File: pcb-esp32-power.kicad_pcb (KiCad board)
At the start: 2 copper layers, 75 x 34 mm, 36 parts, among them IC1 IP5108, IC2 SY8008B, J1 DB9_Female, J2 Conn_01x02, J3 Conn_01x14, J4 Conn_01x16, U1 STEPDOWN12_5

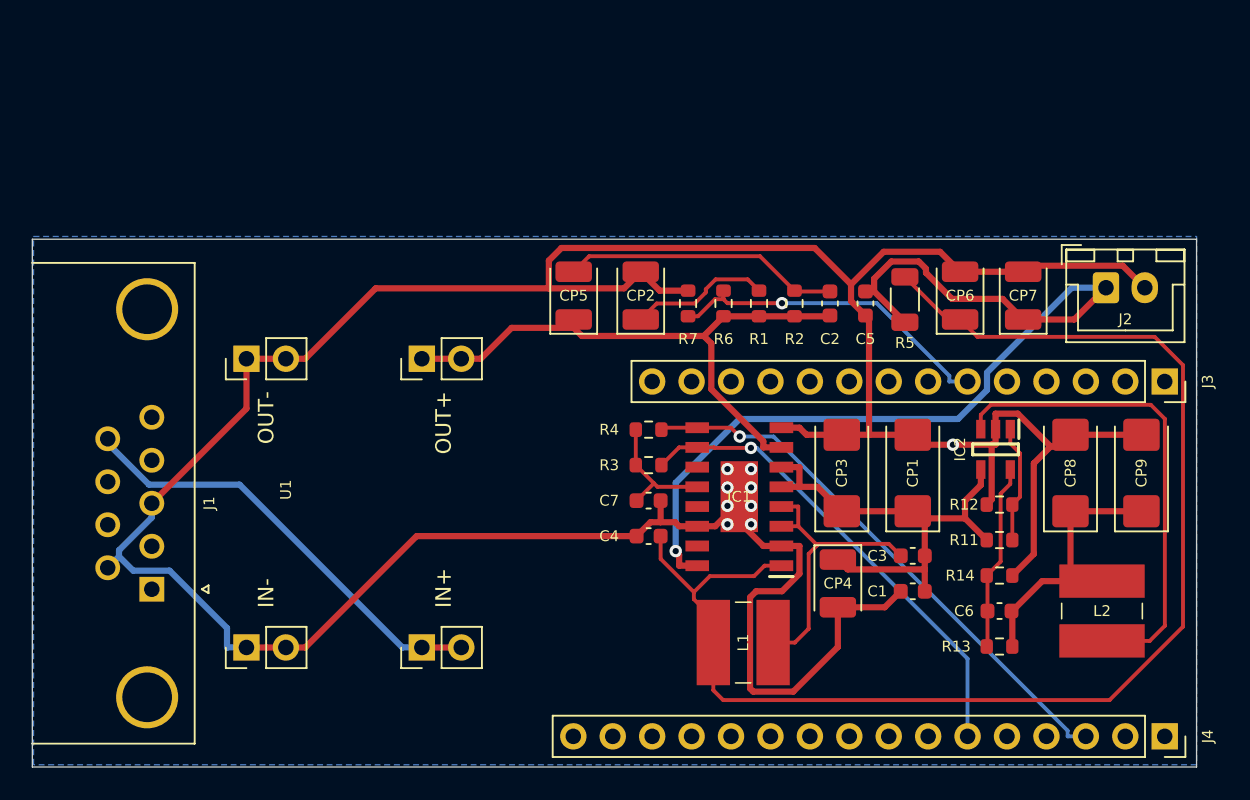
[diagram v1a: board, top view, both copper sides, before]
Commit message: ESP32 Bus verwendet
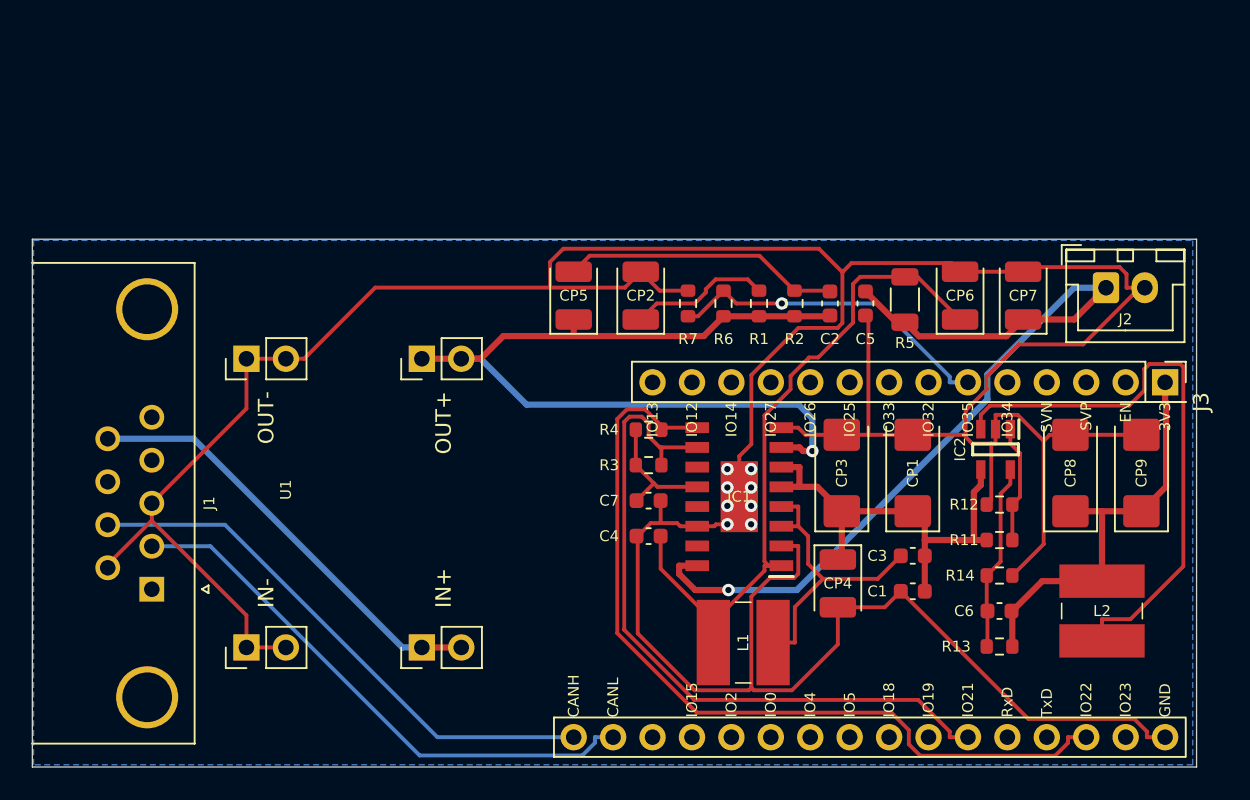
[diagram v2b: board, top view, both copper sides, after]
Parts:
- removed J4: Conn_01x16, Connector_PinSocket_2.54mm:PinSocket_1x16_P2.54mm_Vertical
- J3: value Conn_01x14 -> Bus_Connector; footprint Connector_PinSocket_2.54mm:PinSocket_1x14_P2.54mm_Vertical -> esp32bus:PinHeader
- moved J3 0.06 mm to (173.0, 109.2)
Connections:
- J3 pad 1: Net-(J3-Pad1) -> +3V3
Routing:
- net Net-(C4-Pad1): track 87.3 -> 43.5 mm
- net GND: track 222.2 -> 260.0 mm, vias 9 -> 8
- net CANL: track 0.00 -> 36.0 mm
- net CANH: track 0.00 -> 35.7 mm
- net SCL: track 35.8 -> 54.6 mm, vias 1 -> 0
- net 5VIN: track 38.3 -> 56.9 mm, vias 0 -> 1
- net SDA: track 30.8 -> 45.9 mm, vias 1 -> 0
- net +3V3: track 18.0 -> 27.0 mm
- net Net-(IC2-Pad3): track 31.2 -> 37.1 mm
- net +BATT: track 62.3 -> 56.6 mm
- net 5VOUT: track 31.2 -> 29.0 mm

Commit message: Breite Platine mit SUB D
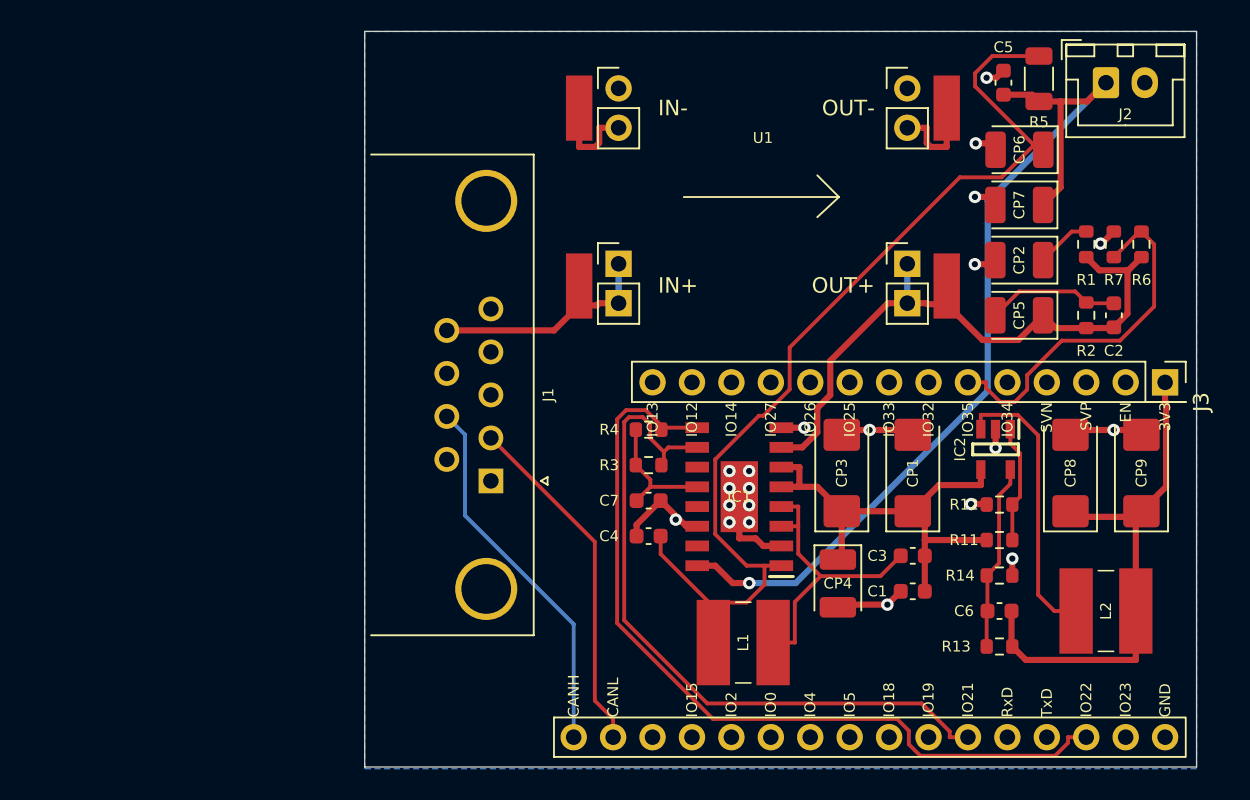
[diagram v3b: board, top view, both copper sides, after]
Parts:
- moved U1 32.9 mm to (147.1, 97.3), turned to 0 degrees
- moved CP5 28.7 mm to (163.6, 104.9), turned to 180 degrees
- moved R7 27.7 mm to (169.7, 100.3)
- moved R6 27.2 mm to (171.4, 100.3)
- moved CP2 24.5 mm to (163.6, 101.3), turned to 180 degrees
- moved J1 22.9 mm to (129.5, 115.6)
- moved R1 21.4 mm to (167.9, 100.3)
- moved R2 18.8 mm to (167.9, 104.9)
- moved C2 18.3 mm to (169.7, 104.9)
- moved C5 16.8 mm to (162.6, 89.9), turned to 90 degrees
- moved R5 16.6 mm to (164.8, 89.7)
- moved J2 13.2 mm to (169.2, 89.9)
- moved CP6 10.1 mm to (163.6, 94.2), turned to 180 degrees
- moved CP7 5.85 mm to (163.6, 97.8), turned to 180 degrees
- moved L2 0.25 mm to (169.2, 124.0), turned to 270 degrees
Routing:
- net GND: track 260.0 -> 51.7 mm, vias 8 -> 21
- net Net-(C4-Pad1): track 43.5 -> 65.3 mm
- net Net-(IC2-Pad3): track 37.1 -> 18.3 mm
- net 5VIN: track 56.9 -> 41.5 mm, vias 1 -> 0
- net CANL: track 36.0 -> 22.5 mm
- net +12V: track 28.3 -> 15.6 mm
- net CANH: track 35.7 -> 24.1 mm
- net Net-(C2-Pad2): track 17.9 -> 8.59 mm
- net +3V3: track 27.0 -> 33.7 mm
- net Net-(CP2-Pad1): track 9.11 -> 3.54 mm
- net +BATT: track 56.6 -> 61.7 mm
- net EXTPOW: track 21.4 -> 23.4 mm, vias 1 -> 0
- net 5VOUT: track 29.0 -> 30.3 mm
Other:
- board size 75 x 34 mm -> 53.6 x 47.4 mm

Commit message: Mit OBD II Stecker
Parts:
- J1: value DB9_Female -> C-OBD-II-16M; footprint Connector_Dsub:DSUB-9_Female_Horizontal_P2.77x2.84mm_EdgePinOffset4.94mm_Housed_MountingHolesOffset7.48mm -> OBD-II:COMTECH_C-OBD-II-16M
- moved J1 19.3 mm to (128.1, 96.3)
- moved J2 3.10 mm to (170.9, 92.5), turned to 270 degrees
- turned C4 to 0 degrees
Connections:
- J1 pad 2: CANL -> Net-(J1-Pad2)
- J1 pad 3: GND -> Net-(J1-Pad3)
- J1 pad 5: Net-(J1-Pad5) -> GND
- J1 pad 6: GND -> CANH
- J1 pad 7: CANH -> Net-(J1-Pad7)
- J1 pad 9: +12V -> Net-(J1-Pad9)
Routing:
- net Net-(C4-Pad1): track 65.3 -> 101.3 mm
- net +12V: track 15.6 -> 29.1 mm, vias 0 -> 1
- net SDA: track 45.6 -> 51.4 mm
- net CANH: track 24.1 -> 19.3 mm
- net CANL: track 22.5 -> 18.4 mm
- net 5VIN: track 41.5 -> 45.2 mm, vias 0 -> 1
- net GND: track 51.7 -> 48.3 mm, vias 21 -> 22
- net SCL: track 54.2 -> 51.1 mm
- net 5VOUT: track 30.3 -> 29.0 mm
- net +BATT: track 61.7 -> 61.2 mm
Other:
- board size 53.6 x 47.4 mm -> 48.6 x 47.4 mm
